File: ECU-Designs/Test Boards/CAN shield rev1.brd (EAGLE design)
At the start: 22 parts

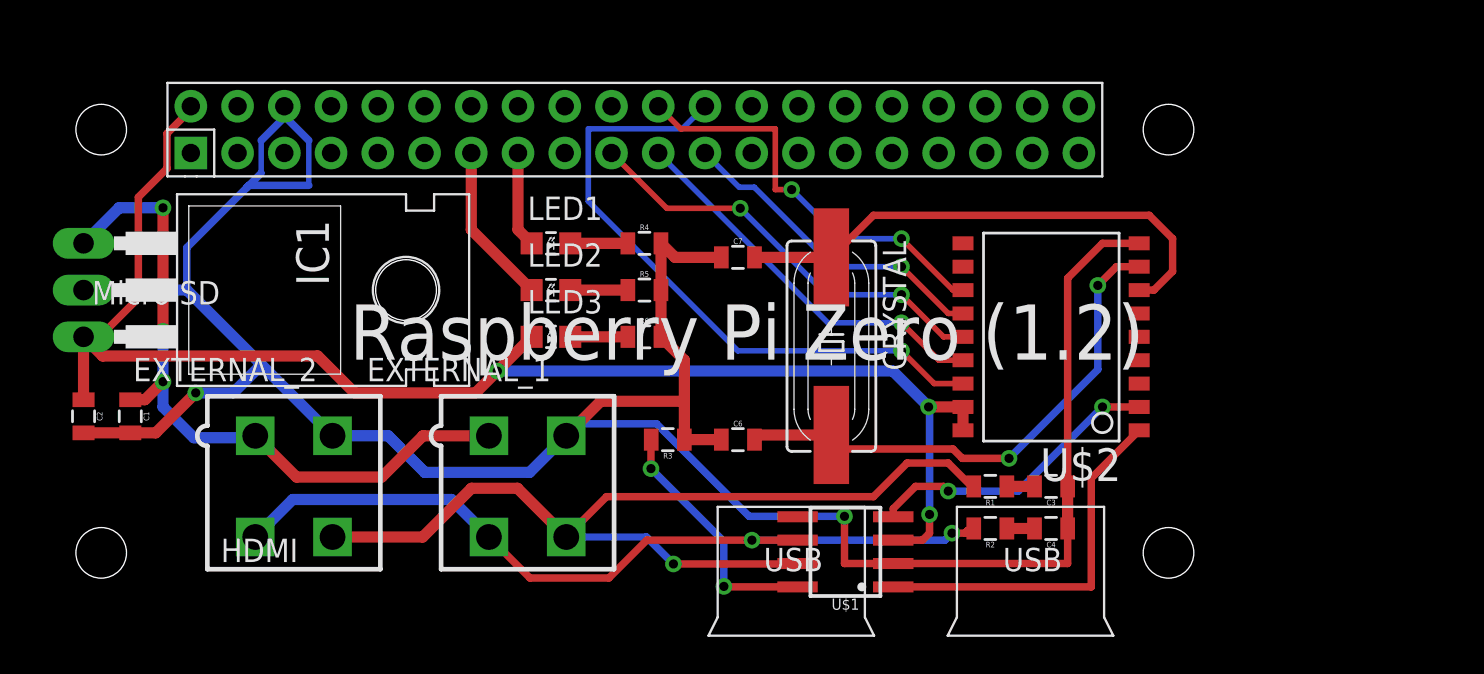
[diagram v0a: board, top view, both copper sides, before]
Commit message: New versions of power board, bspd test board, can shield, bms adapter segment, bms shield
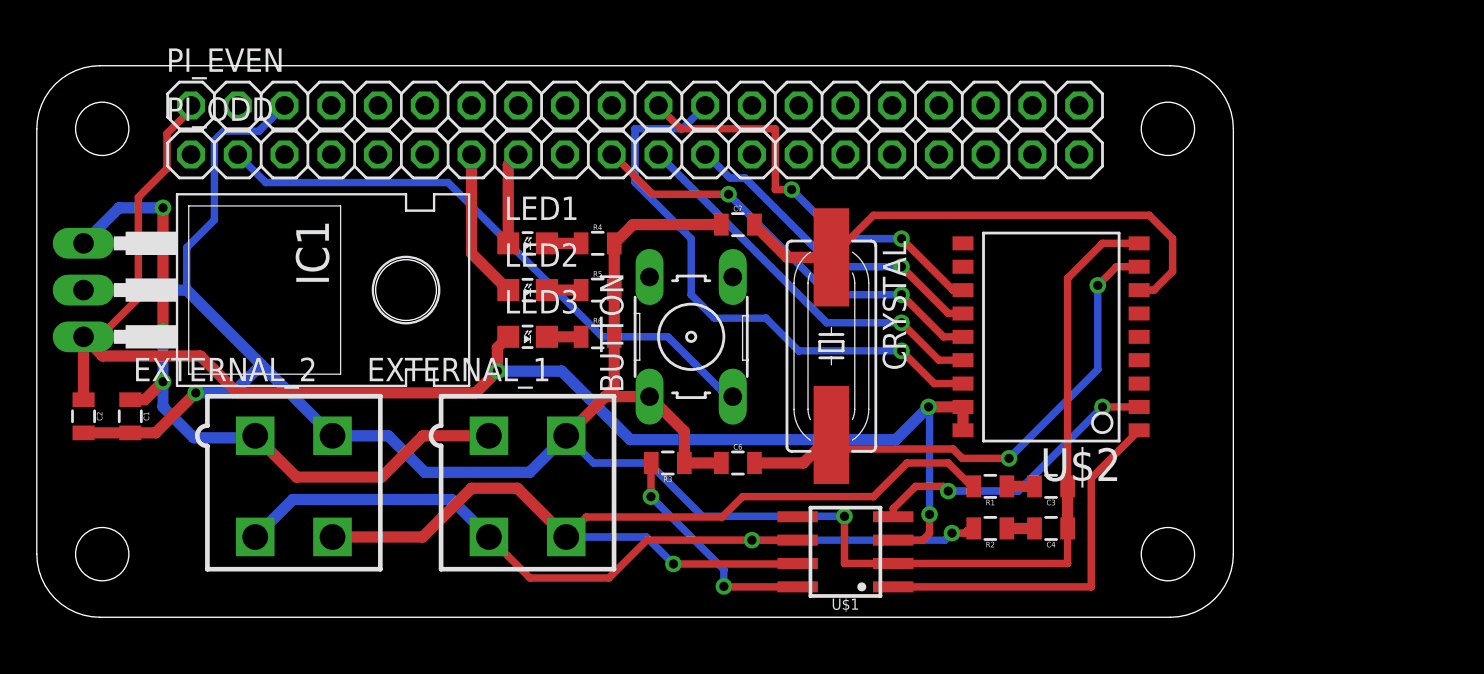
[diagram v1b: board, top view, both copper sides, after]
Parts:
- removed U$3: RASPBERRY_PI_ZERO-V1.2, HyTechDevices:RASPBERRY_PI_ZERO-V1.2
- added BUTTON: (no value), HyTechDevices:B3F-10XX
- added PI_EVEN, PI_ODD: (no value), HyTechDevices:1X20
- C1: value .22uF -> .33uF
- EXTERNAL_1, EXTERNAL_2: value MINIFIT_5566-4 -> (none)
- moved R4 2.54 mm to (30.5, 20.3)
- moved R5 2.54 mm to (30.5, 17.8)
- moved R6 2.54 mm to (30.5, 15.2)
- moved C7 1.78 mm to (38.1, 21.3)
- moved C6 1.27 mm to (38.1, 8.38)
- moved LED1 1.27 mm to (26.7, 20.3)
- moved LED2 1.27 mm to (26.7, 17.8)
- moved LED3 1.27 mm to (26.7, 15.2)
- moved R3 1.27 mm to (34.3, 8.38)
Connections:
- new net BUT: BUTTON.3, PI_ODD.2
- net +5V: now also PI_EVEN.1; no longer U$3.2
- net CS: now also PI_EVEN.12; no longer U$3.24
- net GND: now also BUTTON.1, PI_EVEN.3; no longer U$3.6
- net INT: now also PI_EVEN.11; no longer U$3.22
- net LED1: now also PI_ODD.8; no longer U$3.15
- net LED2: now also PI_ODD.7; no longer U$3.13
- net MISO: now also PI_ODD.11; no longer U$3.21
- net MOSI: now also PI_ODD.10; no longer U$3.19
- net SCK: now also PI_ODD.12; no longer U$3.23
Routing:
- net BUT: track 0.00 -> 32.3 mm
- net GND: track 139.2 -> 134.1 mm
- net CS: track 35.2 -> 31.4 mm
- net N$16: track 13.6 -> 12.4 mm
- net N$7: track 3.13 -> 1.86 mm
- net N$2: track 3.13 -> 1.86 mm
- net N$1: track 3.13 -> 1.86 mm
- net +5V: track 82.1 -> 83.1 mm
- net N$15: track 28.2 -> 28.9 mm
- net LED2: track 8.81 -> 8.19 mm
- net N$11: track 28.5 -> 29.1 mm
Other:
- board outline added: 65 x 30 mm
- board text added: "CAN shield rev1"
- board text added: "Nathan Cheek"
- board text added: "Nothing to see here..."
